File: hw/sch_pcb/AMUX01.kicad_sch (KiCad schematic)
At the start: 18 parts, among them J1 Umin ... Umax, J2 HEADER_1x03, J3 HEADER_1x03, J4 HEADER_1x03, J5 HEADER_1x03, J6 HEADER_2x03_PARALLEL, J7 HEADER_2x01_PARALLEL, J8 HEADER_2x01_PARALLEL, J9 HEADER_1x02, M1 HOLE M3, M2 HOLE M3, M3 HOLE, M4 HOLE, U1 MAX4734EUB+

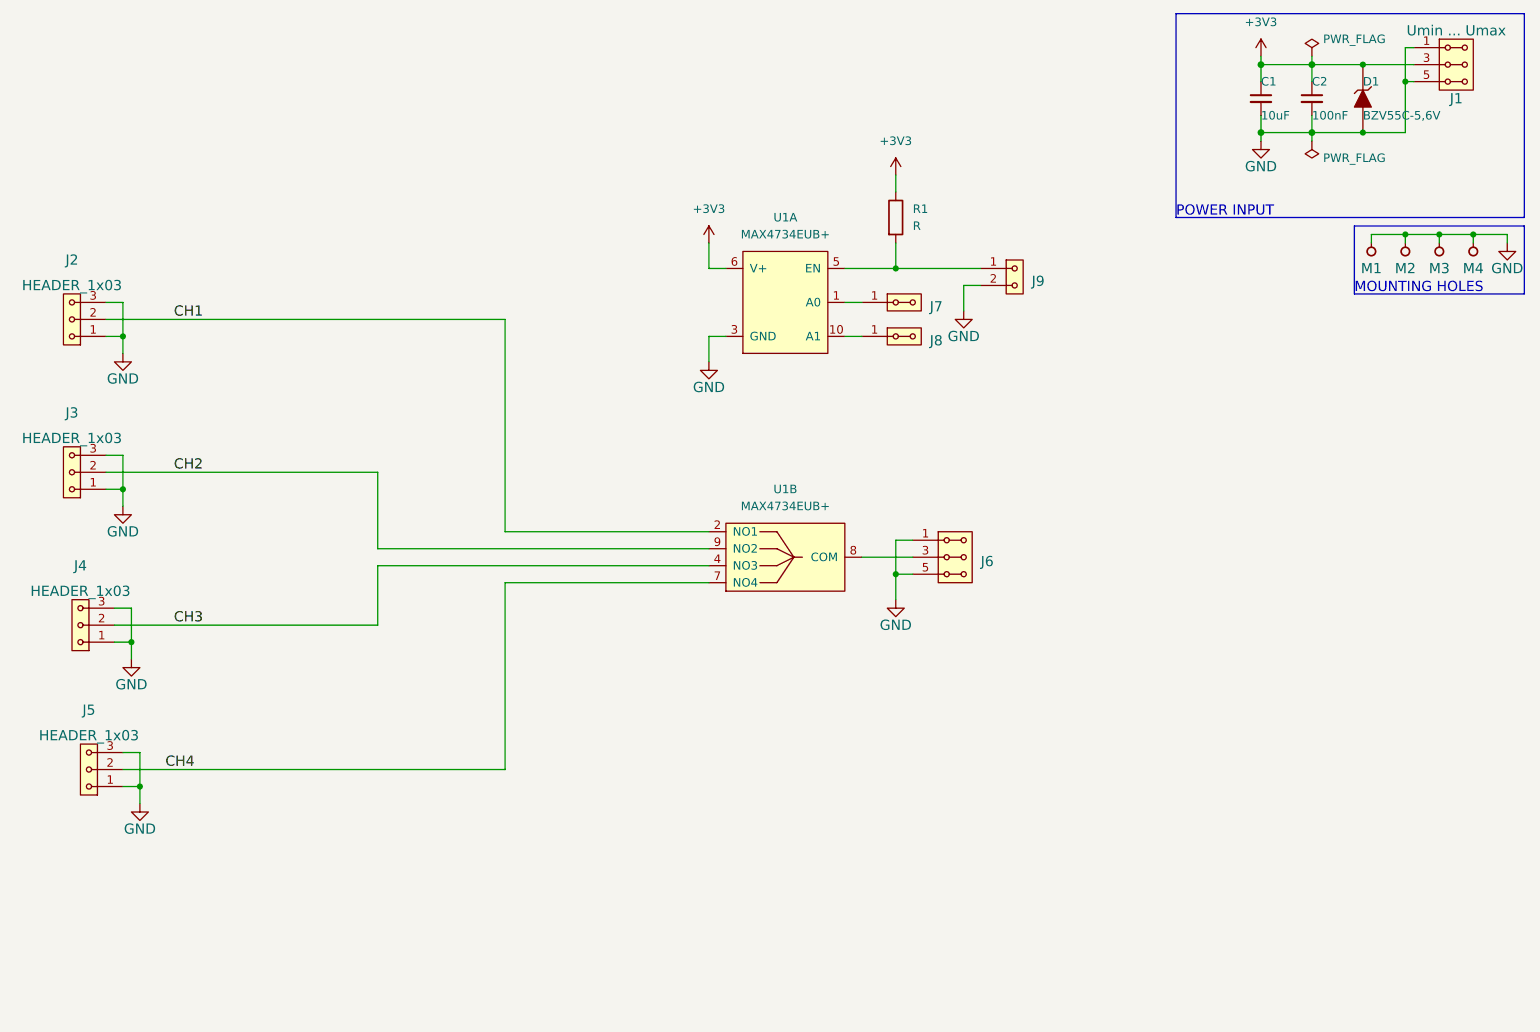
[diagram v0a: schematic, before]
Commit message: Change address setup. Use script to make module layout. Update PCB from schematics.
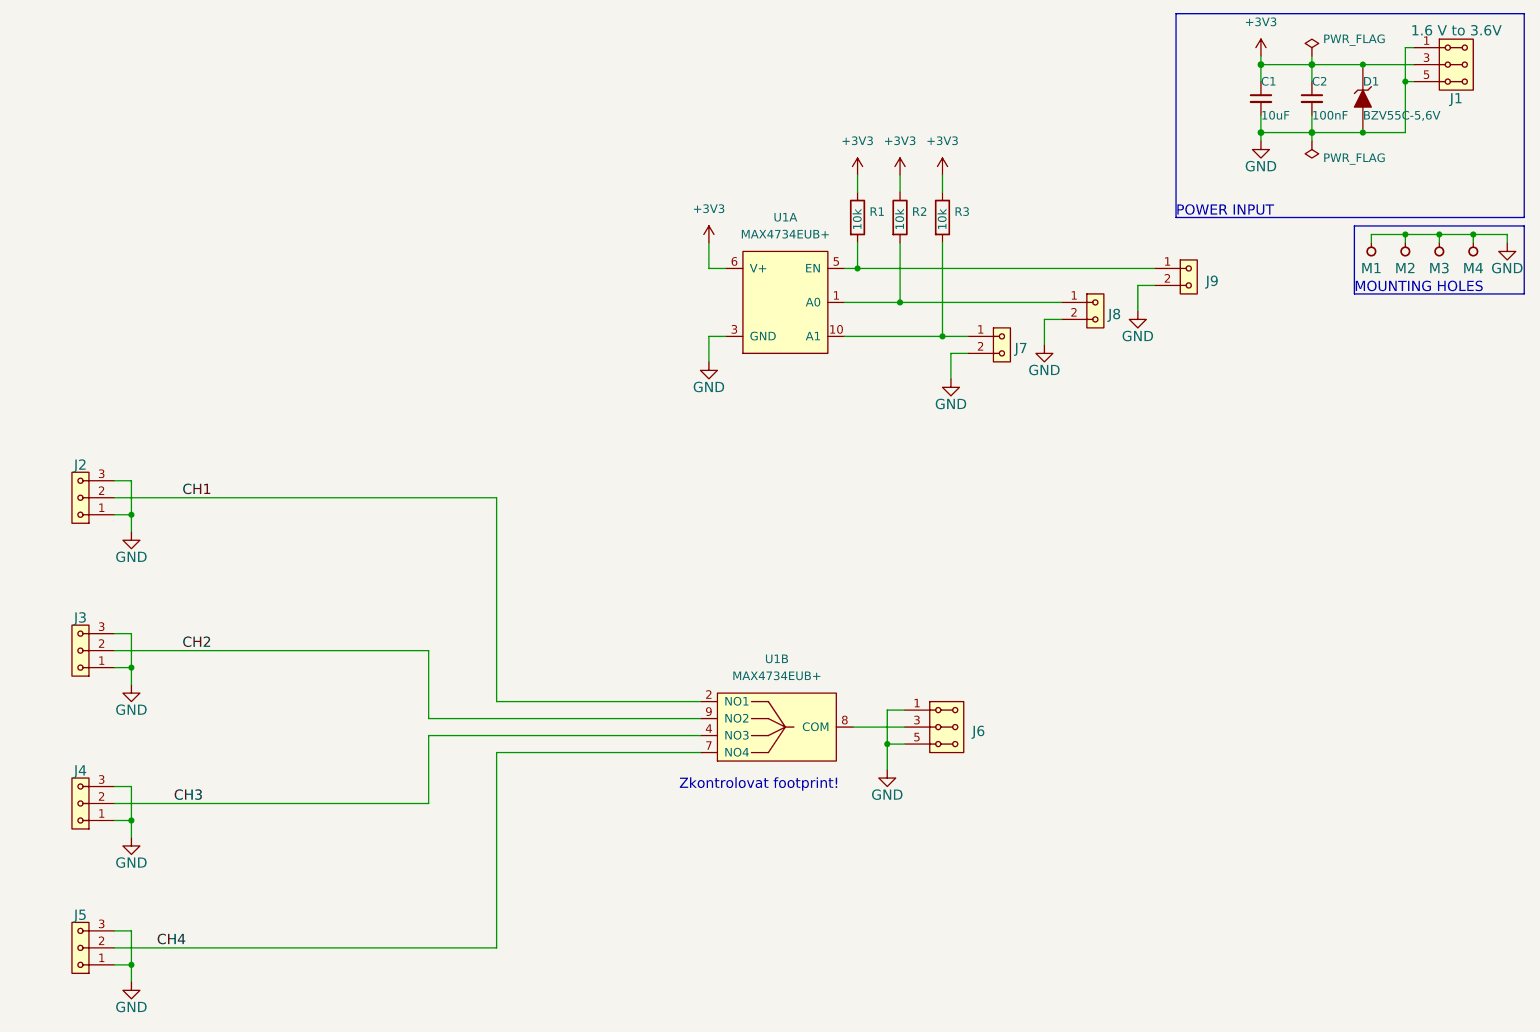
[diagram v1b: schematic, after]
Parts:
- removed J7, J8: HEADER_2x01_PARALLEL, symbol MLAB_HEADER:HEADER_2x01_PARALLEL
- added J7, J8: HEADER_1x02, Mlab_Pin_Headers:Straight_2x01, symbol MLAB_HEADER:HEADER_1x02
- added R2, R3: 10k, Resistor_SMD:R_0805_2012Metric, symbol Device:R
- J1: value Umin ... Umax -> 1.6 V to 3.6V
- J9: footprint (none) -> Mlab_Pin_Headers:Straight_2x01
- R1: value R -> 10k; footprint (none) -> Resistor_SMD:R_0805_2012Metric
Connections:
- net +3V3: now also R2.1, R3.1
- net GND: now also J7.2, J8.2
- net at U1.1 (A0): now also J8.1, R2.2
- net at U1.10 (A1): now also J7.1, R3.2
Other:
- note added: "Zkontrolovat footprint!"
- moved on the sheet: J2, J3, J4, J5, J6, J9, R1, U1B
